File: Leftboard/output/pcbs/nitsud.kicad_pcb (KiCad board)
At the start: 2 copper layers, 137 x 99 mm, 63 parts

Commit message: figured .yaml is needed
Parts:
- added H1: , ceoloide:mounting_hole_plated, F.Cu at (159.5, 102.5)
- added H2: , ceoloide:mounting_hole_plated, F.Cu at (159.5, 140.5)
- added H3: , ceoloide:mounting_hole_plated, F.Cu at (235.5, 102.5)
- added H4: , ceoloide:mounting_hole_plated, F.Cu at (235.5, 159.5)
- moved D27 38.0 mm to (188.0, 174.0)
- moved D29 38.0 mm to (226.0, 174.0)
- moved S27 38.0 mm to (188.0, 169.0)
- moved S29 38.0 mm to (226.0, 169.0)
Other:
- outline, holes or cut-outs redrawn
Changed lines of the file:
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@@
           )
       (module MX (layer F.Cu)
-      (at 226 169 0)
+      (at 188 169 0)
       (fp_text reference "S27" (at 0 0) (layer F.SilkS) hide (effects (font (size 1.27 1.27) (thickness 0.15))))
       (fp_text value "" (at 0 0) (layer F.SilkS) hide (effects (font (size 1.27 1.27) (thickness 0.15))))
@@
           )
       (module MX (layer F.Cu)
-      (at 188 169 0)
+      (at 226 169 0)
       (fp_text reference "S29" (at 0 0) (layer F.SilkS) hide (effects (font (size 1.27 1.27) (thickness 0.15))))
       (fp_text value "" (at 0 0) (layer F.SilkS) hide (effects (font (size 1.27 1.27) (thickness 0.15))))
@@
     )
     (module ComboDiode (layer F.Cu)
-        (at 226 174 0)
+        (at 188 174 0)
         (fp_text reference "D27" (at 0 0) (layer F.SilkS) hide (effects (font (size 1.27 1.27) (thickness 0.15))))
         (fp_text value "" (at 0 0) (layer F.SilkS) hide (effects (font (size 1.27 1.27) (thickness 0.15))))
@@
     )
     (module ComboDiode (layer F.Cu)
-        (at 188 174 0)
+        (at 226 174 0)
         (fp_text reference "D29" (at 0 0) (layer F.SilkS) hide (effects (font (size 1.27 1.27) (thickness 0.15))))
         (fp_text value "" (at 0 0) (layer F.SilkS) hide (effects (font (size 1.27 1.27) (thickness 0.15))))
@@
         (pad 2 smd rect (at 3.1 1.85 -90) (size 1.8 1.1) (layers F.Cu F.Paste F.Mask) (net 33 "RST"))
     )
+  (footprint "ceoloide:mounting_hole_plated"
+    (layer "F.Cu")
+    (at 159.5 102.5 0)
+    (property "Reference" "H1"
+      (at 0 3 0)
+      (layer "F.SilkS")
+      hide
+      (effects (font (size 1 1) (thickness 0.15)))
+    )
+    (pad "" thru_hole circle (at 0 0 0) (size 3.8000000000000003 3.8000000000000003) (drill 2.2) (layers "*.Cu" "*.Mask"))
+    (fp_circle (center 0 0) (end -2.1500000000000004 0) (layer "F.CrtYd") (stroke (width 0.05) (type solid)) (fill none))
+    (fp_circle (center 0 0) (end -2.1500000000000004 0) (layer "B.CrtYd") (stroke (width 0.05) (type solid)) (fill none))
+  )
+  (footprint "ceoloide:mounting_hole_plated"
+    (layer "F.Cu")
+    (at 159.5 140.5 0)
+    (property "Reference" "H2"
+      (at 0 3 0)
+      (layer "F.SilkS")
+      hide
+      (effects (font (size 1 1) (thickness 0.15)))
+    )
+    (pad "" thru_hole circle (at 0 0 0) (size 3.8000000000000003 3.8000000000000003) (drill 2.2) (layers "*.Cu" "*.Mask"))
+    (fp_circle (center 0 0) (end -2.1500000000000004 0) (layer "F.CrtYd") (stroke (width 0.05) (type solid)) (fill none))
+    (fp_circle (center 0 0) (end -2.1500000000000004 0) (layer "B.CrtYd") (stroke (width 0.05) (type solid)) (fill none))
+  )
+  (footprint "ceoloide:mounting_hole_plated"
+    (layer "F.Cu")
+    (at 235.5 102.5 0)
+    (property "Reference" "H3"
+      (at 0 3 0)
+      (layer "F.SilkS")
+      hide
+      (effects (font (size 1 1) (thickness 0.15)))
+    )
+    (pad "" thru_hole circle (at 0 0 0) (size 3.8000000000000003 3.8000000000000003) (drill 2.2) (layers "*.Cu" "*.Mask"))
+    (fp_circle (center 0 0) (end -2.1500000000000004 0) (layer "F.CrtYd") (stroke (width 0.05) (type solid)) (fill none))
+    (fp_circle (center 0 0) (end -2.1500000000000004 0) (layer "B.CrtYd") (stroke (width 0.05) (type solid)) (fill none))
+  )
+  (footprint "ceoloide:mounting_hole_plated"
+    (layer "F.Cu")
+    (at 235.5 159.5 0)
+    (property "Reference" "H4"
+      (at 0 3 0)
+      (layer "F.SilkS")
+      hide
+      (effects (font (size 1 1) (thickness 0.15)))
+    )
+    (pad "" thru_hole circle (at 0 0 0) (size 3.8000000000000003 3.8000000000000003) (drill 2.2) (layers "*.Cu" "*.Mask"))
+    (fp_circle (center 0 0) (end -2.1500000000000004 0) (layer "F.CrtYd") (stroke (width 0.05) (type solid)) (fill none))
+    (fp_circle (center 0 0) (end -2.1500000000000004 0) (layer "B.CrtYd") (stroke (width 0.05) (type solid)) (fill none))
+  )
   (gr_line (start 138.5 82.5) (end 138.5 160.5) (angle 90) (layer Edge.Cuts) (width 0.15))
 (gr_line (start 139.5 161.5) (end 175.5 161.5) (angle 90) (layer Edge.Cuts) (width 0.15))
 (gr_line (start 176.5 162.5) (end 176.5 179.5) (angle 90) (layer Edge.Cuts) (width 0.15))
-(gr_line (start 177.5 180.5) (end 274.5 180.5) (angle 90) (layer Edge.Cuts) (width 0.15))
-(gr_line (start 275.5 179.5) (end 275.5 82.5) (angle 90) (layer Edge.Cuts) (width 0.15))
-(gr_line (start 274.5 81.5) (end 139.5 81.5) (angle 90) (layer Edge.Cuts) (width 0.15))
+(gr_line (start 177.5 180.5) (end 274.5048360387049 180.5) (angle 90) (layer Edge.Cuts) (width 0.15))
+(gr_line (start 275.5048360387049 179.49983610003255) (end 275.5000000007179 150.00000437907875) (angle 90) (layer Edge.Cuts) (width 0.15))
+(gr_line (start 275.5000000007179 149.99983608722687) (end 275.5002956204186 82.50000441074371) (angle 90) (layer Edge.Cuts) (width 0.15))
+(gr_line (start 274.5002956204186 81.5) (end 139.5 81.5) (angle 90) (layer Edge.Cuts) (width 0.15))
 (gr_arc (start 139.5 160.5) (end 138.5 160.5) (angle -90) (layer Edge.Cuts) (width 0.15))
 (gr_arc (start 175.5 162.5) (end 176.5 162.5) (angle -90) (layer Edge.Cuts) (width 0.15))
 (gr_arc (start 177.5 179.5) (end 176.5 179.5) (angle -90) (layer Edge.Cuts) (width 0.15))
-(gr_arc (start 274.5 179.5) (end 274.5 180.5) (angle -90) (layer Edge.Cuts) (width 0.15))
-(gr_arc (start 274.5 82.5) (end 275.5 82.5) (angle -90) (layer Edge.Cuts) (width 0.15))
+(gr_arc (start 274.5048360387049 179.5) (end 274.5048360387049 180.5) (angle -90.00939077631294) (layer Edge.Cuts) (width 0.15))
+(gr_arc (start 276.50000000071793 149.99984047934413) (end 275.50000000071793 149.99983607934413) (angle -0.00964241275497102) (layer Edge.Cuts) (width 0.15))
+(gr_arc (start 274.5002956204186 82.50000000745058) (end 275.5002956204186 82.50000440745058) (angle -90.00025229011248) (layer Edge.Cuts) (width 0.15))
 (gr_arc (start 139.5 82.5) (end 139.5 81.5) (angle -90) (layer Edge.Cuts) (width 0.15))
 )

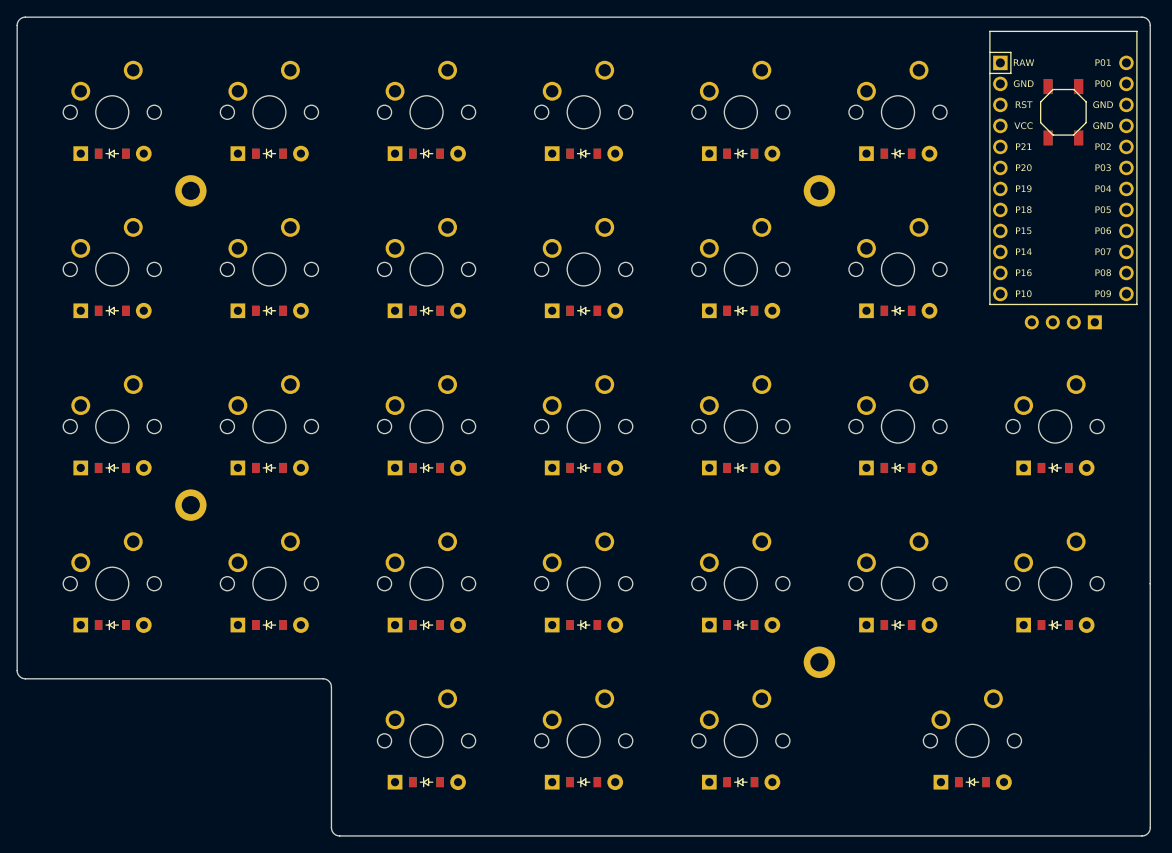
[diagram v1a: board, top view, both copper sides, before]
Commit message: added reset, led, trrs
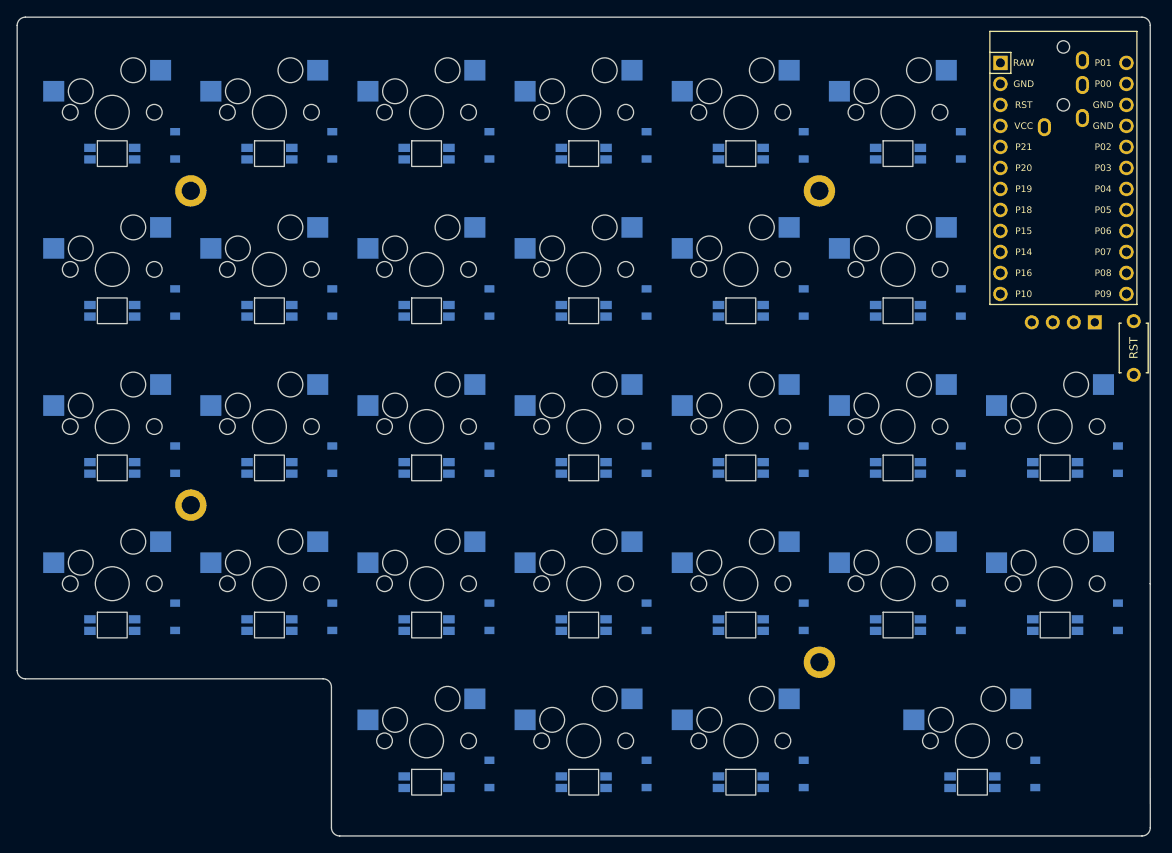
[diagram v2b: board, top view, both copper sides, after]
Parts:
- removed B1: , E73:SW_TACT_ALPS_SKQGABE010
- added LED1: , ceoloide:led_SK6812mini-e (per-keysingle-side), B.Cu at (150.0, 155.0)
- added LED10: , ceoloide:led_SK6812mini-e (per-keysingle-side), B.Cu at (188.0, 136.0)
- added LED11: , ceoloide:led_SK6812mini-e (per-keysingle-side), B.Cu at (188.0, 117.0)
- added LED12: , ceoloide:led_SK6812mini-e (per-keysingle-side), B.Cu at (188.0, 98.0)
- added LED13: , ceoloide:led_SK6812mini-e (per-keysingle-side), B.Cu at (207.0, 155.0)
- added LED14: , ceoloide:led_SK6812mini-e (per-keysingle-side), B.Cu at (207.0, 136.0)
- added LED15: , ceoloide:led_SK6812mini-e (per-keysingle-side), B.Cu at (207.0, 117.0)
- added LED16: , ceoloide:led_SK6812mini-e (per-keysingle-side), B.Cu at (207.0, 98.0)
- added LED17: , ceoloide:led_SK6812mini-e (per-keysingle-side), B.Cu at (226.0, 155.0)
- added LED18: , ceoloide:led_SK6812mini-e (per-keysingle-side), B.Cu at (226.0, 136.0)
- added LED19: , ceoloide:led_SK6812mini-e (per-keysingle-side), B.Cu at (226.0, 117.0)
- added LED2: , ceoloide:led_SK6812mini-e (per-keysingle-side), B.Cu at (150.0, 136.0)
- added LED20: , ceoloide:led_SK6812mini-e (per-keysingle-side), B.Cu at (226.0, 98.0)
- added LED21: , ceoloide:led_SK6812mini-e (per-keysingle-side), B.Cu at (245.0, 155.0)
- added LED22: , ceoloide:led_SK6812mini-e (per-keysingle-side), B.Cu at (245.0, 136.0)
- added LED23: , ceoloide:led_SK6812mini-e (per-keysingle-side), B.Cu at (245.0, 117.0)
- added LED24: , ceoloide:led_SK6812mini-e (per-keysingle-side), B.Cu at (245.0, 98.0)
- added LED25: , ceoloide:led_SK6812mini-e (per-keysingle-side), B.Cu at (264.0, 155.0)
- added LED26: , ceoloide:led_SK6812mini-e (per-keysingle-side), B.Cu at (264.0, 136.0)
- added LED27: , ceoloide:led_SK6812mini-e (per-keysingle-side), B.Cu at (188.0, 174.0)
- added LED28: , ceoloide:led_SK6812mini-e (per-keysingle-side), B.Cu at (207.0, 174.0)
- added LED29: , ceoloide:led_SK6812mini-e (per-keysingle-side), B.Cu at (226.0, 174.0)
- added LED3: , ceoloide:led_SK6812mini-e (per-keysingle-side), B.Cu at (150.0, 117.0)
- added LED30: , ceoloide:led_SK6812mini-e (per-keysingle-side), B.Cu at (254.0, 174.0)
- added LED4: , ceoloide:led_SK6812mini-e (per-keysingle-side), B.Cu at (150.0, 98.0)
- added LED5: , ceoloide:led_SK6812mini-e (per-keysingle-side), B.Cu at (169.0, 155.0)
- added LED6: , ceoloide:led_SK6812mini-e (per-keysingle-side), B.Cu at (169.0, 136.0)
- added LED7: , ceoloide:led_SK6812mini-e (per-keysingle-side), B.Cu at (169.0, 117.0)
- added LED8: , ceoloide:led_SK6812mini-e (per-keysingle-side), B.Cu at (169.0, 98.0)
- added LED9: , ceoloide:led_SK6812mini-e (per-keysingle-side), B.Cu at (188.0, 155.0)
- added RST1: , ceoloide:reset_switch_tht_top, F.Cu at (273.5, 121.5)
- added TRRS1: , ceoloide:trrs_pj320a, F.Cu at (265.0, 83.5)
- D1, D10, D11, D12, D13, D14, D15, D16, D17, D18, D19, D2, D20, D21, D22, D23, D24, D25, D26, D27, D28, D29, D3, D30, D4, D5, D6, D7, D8, D9: footprint ComboDiode -> ceoloide:diode_tht_sod123; moved to B.Cu
- S1, S10, S11, S12, S13, S14, S15, S16, S17, S18, S19, S2, S20, S21, S22, S23, S24, S25, S26, S27, S28, S29, S3, S30, S4, S5, S6, S7, S8, S9: footprint MX -> ceoloide:switch_mx; moved to B.Cu
- moved D25 7.67 mm to (271.6, 154.0), turned to 90 degrees
- moved D26 7.67 mm to (271.6, 135.0), turned to 90 degrees
- moved D30 7.67 mm to (261.6, 173.0), turned to 90 degrees
- moved D1 7.67 mm to (157.6, 154.0), turned to 90 degrees
- moved D10 7.67 mm to (195.6, 135.0), turned to 90 degrees
- moved D11 7.67 mm to (195.6, 116.0), turned to 90 degrees
- moved D12 7.67 mm to (195.6, 97.0), turned to 90 degrees
- moved D13 7.67 mm to (214.6, 154.0), turned to 90 degrees
- moved D14 7.67 mm to (214.6, 135.0), turned to 90 degrees
- moved D15 7.67 mm to (214.6, 116.0), turned to 90 degrees
- moved D16 7.67 mm to (214.6, 97.0), turned to 90 degrees
- moved D17 7.67 mm to (233.6, 154.0), turned to 90 degrees
- moved D18 7.67 mm to (233.6, 135.0), turned to 90 degrees
- moved D19 7.67 mm to (233.6, 116.0), turned to 90 degrees
- moved D2 7.67 mm to (157.6, 135.0), turned to 90 degrees
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
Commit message: routing time
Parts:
- added G***: LOGO, Graphics:white, F.Cu at (269.0, 170.5)
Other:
- copper layers 2 -> 4
- net class Default removed
- board text added: "nitsud60"

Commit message: routing
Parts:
- removed G***: LOGO, Graphics:white
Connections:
- LED1 pad 2: P10 -> (no net)
- LED1 pad 4: P11 -> (no net)
- LED10 pad 2: P10 -> (no net)
- LED10 pad 4: P11 -> (no net)
- LED11 pad 2: P10 -> (no net)
- LED11 pad 4: P11 -> (no net)
- LED12 pad 2: P10 -> (no net)
- LED12 pad 4: P11 -> (no net)
- LED13 pad 2: P10 -> (no net)
- LED13 pad 4: P11 -> (no net)
- LED14 pad 2: P10 -> (no net)
- LED14 pad 4: P11 -> (no net)
- LED15 pad 2: P10 -> (no net)
- LED15 pad 4: P11 -> (no net)
- LED16 pad 2: P10 -> (no net)
- LED16 pad 4: P11 -> (no net)
- LED17 pad 2: P10 -> (no net)
- LED17 pad 4: P11 -> (no net)
- LED18 pad 2: P10 -> (no net)
- LED18 pad 4: P11 -> (no net)
- LED19 pad 2: P10 -> (no net)
- LED19 pad 4: P11 -> (no net)
- LED2 pad 2: P10 -> (no net)
- LED2 pad 4: P11 -> (no net)
- LED20 pad 2: P10 -> (no net)
- LED20 pad 4: P11 -> (no net)
- LED21 pad 2: P10 -> (no net)
- LED21 pad 4: P11 -> (no net)
- LED22 pad 2: P10 -> (no net)
- LED22 pad 4: P11 -> (no net)
- LED23 pad 2: P10 -> (no net)
- LED23 pad 4: P11 -> (no net)
- LED24 pad 2: P10 -> (no net)
- LED24 pad 4: P11 -> (no net)
- LED25 pad 2: P10 -> (no net)
- LED25 pad 4: P11 -> (no net)
- LED26 pad 2: P10 -> (no net)
- LED26 pad 4: P11 -> (no net)
- LED27 pad 2: P10 -> (no net)
- LED27 pad 4: P11 -> (no net)
- LED28 pad 2: P10 -> (no net)
- LED28 pad 4: P11 -> (no net)
- LED29 pad 2: P10 -> (no net)
- LED29 pad 4: P11 -> (no net)
- LED3 pad 2: P10 -> (no net)
- LED3 pad 4: P11 -> (no net)
- LED30 pad 2: P10 -> (no net)
- LED30 pad 4: P11 -> (no net)
- LED4 pad 2: P10 -> (no net)
- LED4 pad 4: P11 -> (no net)
- LED5 pad 2: P10 -> (no net)
- LED5 pad 4: P11 -> (no net)
- LED6 pad 2: P10 -> (no net)
- LED6 pad 4: P11 -> (no net)
- LED7 pad 2: P10 -> (no net)
- LED7 pad 4: P11 -> (no net)
- LED8 pad 2: P10 -> (no net)
- LED8 pad 4: P11 -> (no net)
- LED9 pad 2: P10 -> (no net)
- LED9 pad 4: P11 -> (no net)
- OLED1 pad 3: P3 -> P9
- OLED1 pad 4: P2 -> P8
- S12 pad 1: (no net) -> P19
- S16 pad 1: (no net) -> P18
- S20 pad 1: (no net) -> P15
- S24 pad 1: (no net) -> P14
- S26 pad 1: (no net) -> P16
- S4 pad 1: (no net) -> P21
- S8 pad 1: (no net) -> P20
- TRRS1 pad 2: SL -> GND
- TRRS1 pad 3: R2 -> P1
- TRRS1 pad 4: TP -> RAW
- TRRS1 pad 5: R1 -> P0
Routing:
- net GND: track 0.00 -> 745.0 mm, vias 0 -> 31
- net VCC: track 0.00 -> 672.2 mm, vias 0 -> 30
- net (no net): track 0.00 -> 549.7 mm, vias 0 -> 45
- net P21: track 0.00 -> 189.8 mm, vias 0 -> 1
- net P19: track 0.00 -> 174.1 mm, vias 0 -> 1
- net P20: track 0.00 -> 172.4 mm, vias 0 -> 1
- net P18: track 0.00 -> 156.7 mm, vias 0 -> 1
- net P15: track 0.00 -> 139.2 mm, vias 0 -> 1
- net P14: track 0.00 -> 102.7 mm, vias 0 -> 1
- net RST: track 0.00 -> 66.9 mm, vias 0 -> 1
- net P16: track 0.00 -> 61.1 mm, vias 0 -> 1
- net P0: track 0.00 -> 25.6 mm
- net RAW: track 0.00 -> 15.6 mm
- net P8: track 0.00 -> 13.9 mm
- net P1: track 0.00 -> 12.1 mm
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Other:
- board text removed: "nitsud60"

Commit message: Gerbers Created and added fix to edgecut
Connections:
- D23 pad 1: (no net) -> P3
- D24 pad 1: (no net) -> P2
- D25 pad 1: (no net) -> P5
- D26 pad 1: (no net) -> P4
- D30 pad 1: (no net) -> P6
- LED24 pad 4: (no net) -> P10
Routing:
- net (no net): track 549.7 -> 803.0 mm, vias 45 -> 59
- net P5: track 0.00 -> 205.1 mm, vias 0 -> 9
- net P4: track 0.00 -> 188.4 mm, vias 0 -> 13
- net P2: track 0.00 -> 157.9 mm, vias 0 -> 11
- net P6: track 0.00 -> 150.0 mm, vias 0 -> 1
- net P3: track 0.00 -> 145.7 mm, vias 0 -> 11
- net P10: track 0.00 -> 26.9 mm, vias 0 -> 1
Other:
- outline, holes or cut-outs redrawn
